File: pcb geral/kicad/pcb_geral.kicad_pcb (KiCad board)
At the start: 2 copper layers, 138 x 57 mm, 8 parts

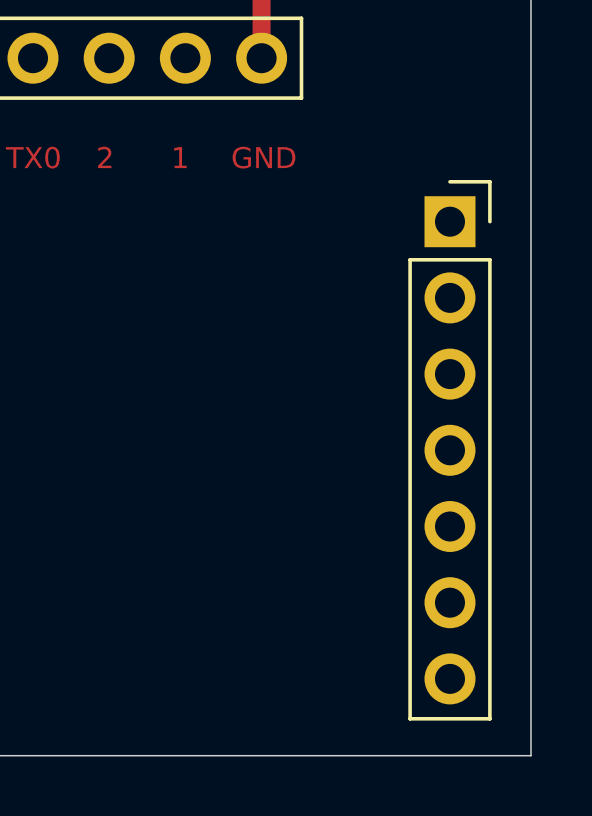
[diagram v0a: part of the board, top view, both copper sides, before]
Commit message: Corrected PCB
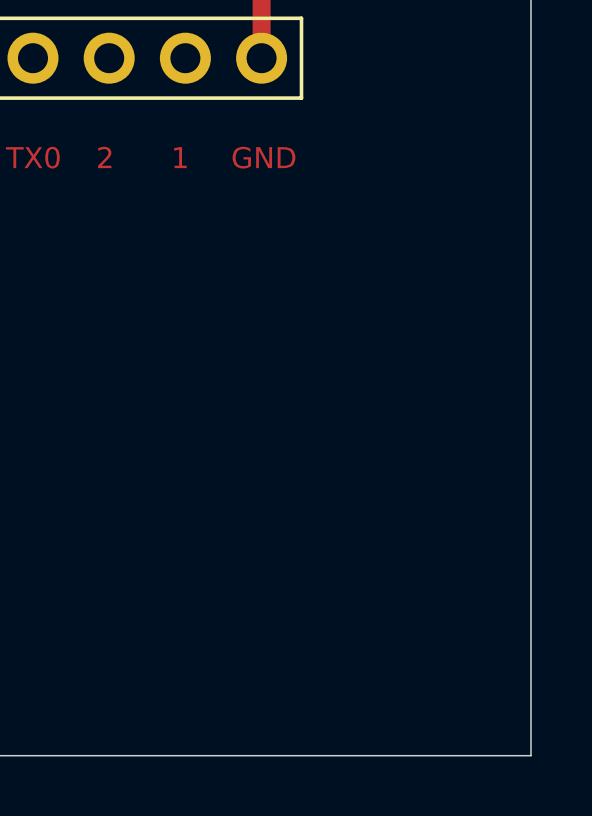
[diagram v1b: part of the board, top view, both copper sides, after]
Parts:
- removed the REF** at (214.8, 115.2)

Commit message: Backup
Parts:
- added REF**: PinSocket_1x07_P2.54mm_Vertical, Connector_PinSocket_2.54mm:PinSocket_1x07_P2.54mm_Vertical, F.Cu at (214.8, 115.2)
